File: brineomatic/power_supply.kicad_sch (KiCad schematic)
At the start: 26 parts, among them J8 5.08MM, J9 5.08MM, Q3 20N06, U2 LM74700, U3 XL1509-5.0

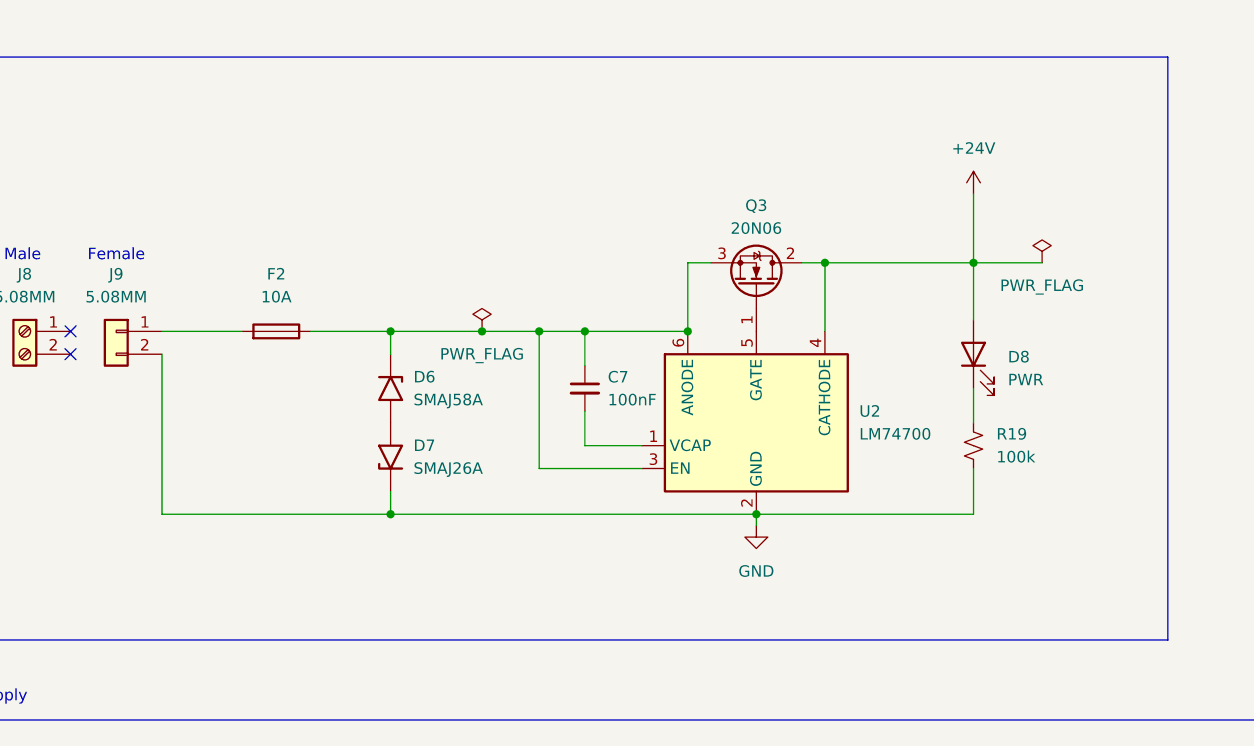
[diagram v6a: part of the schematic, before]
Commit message: removed the onboard fuse.
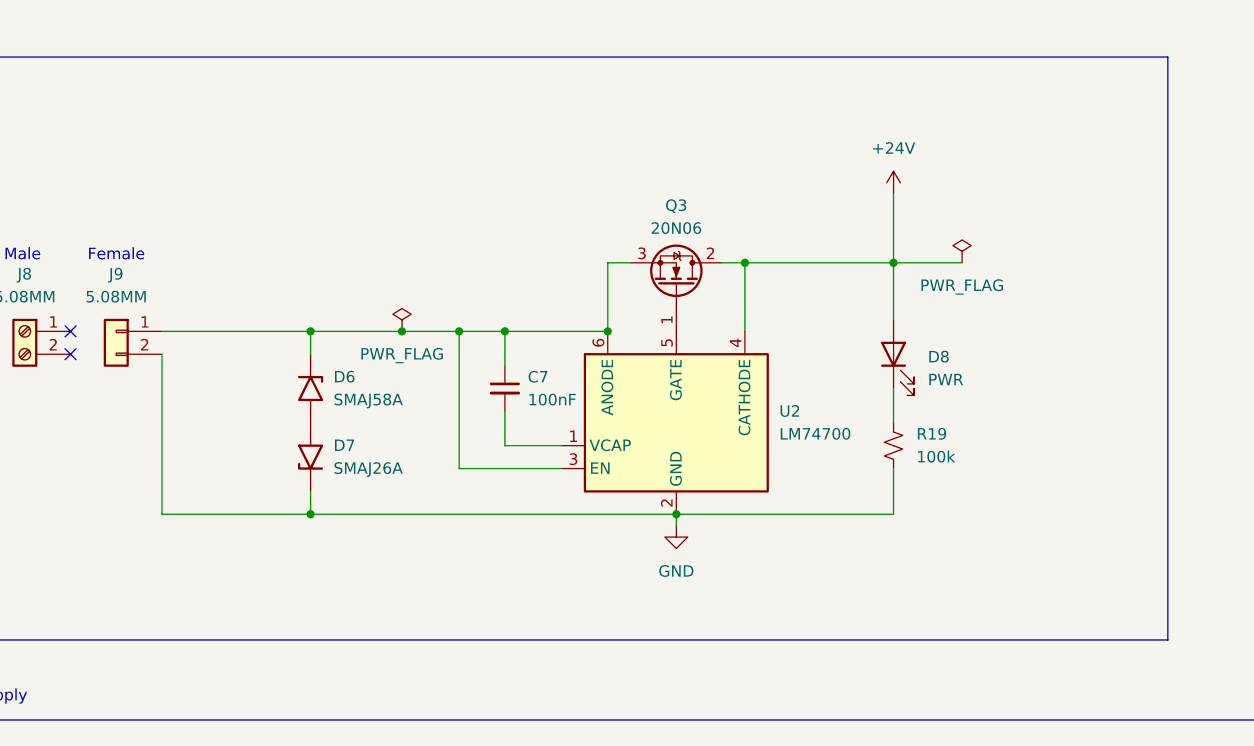
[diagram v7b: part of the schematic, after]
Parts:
- removed F2: 10A, yarrboard:FUSE-TH_XF-508P-A-B, symbol Device:Fuse
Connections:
- net at C7.1, D6.1 (A1), Q3.3 (S)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: now also J9.1 (Pin_1)
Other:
- moved on the sheet: C7, D6, D7, D8, Q3, R19, U2

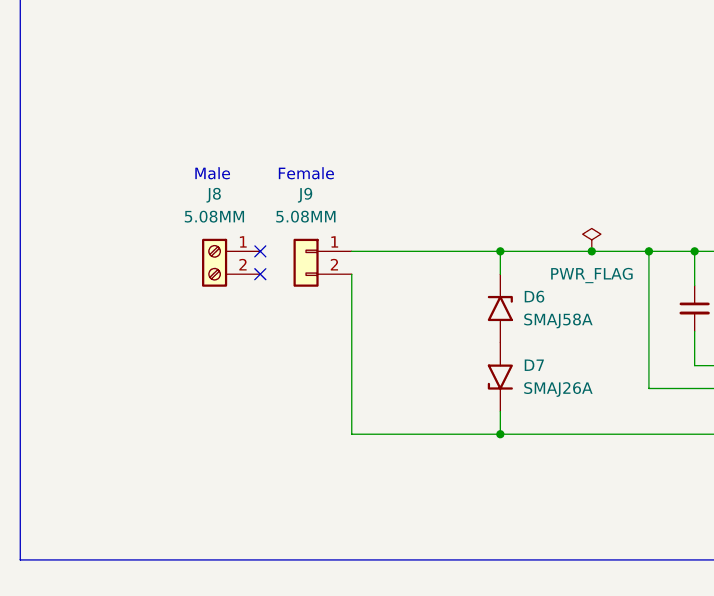
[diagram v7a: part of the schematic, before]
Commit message: re-added fuse, switched to 5x20mm
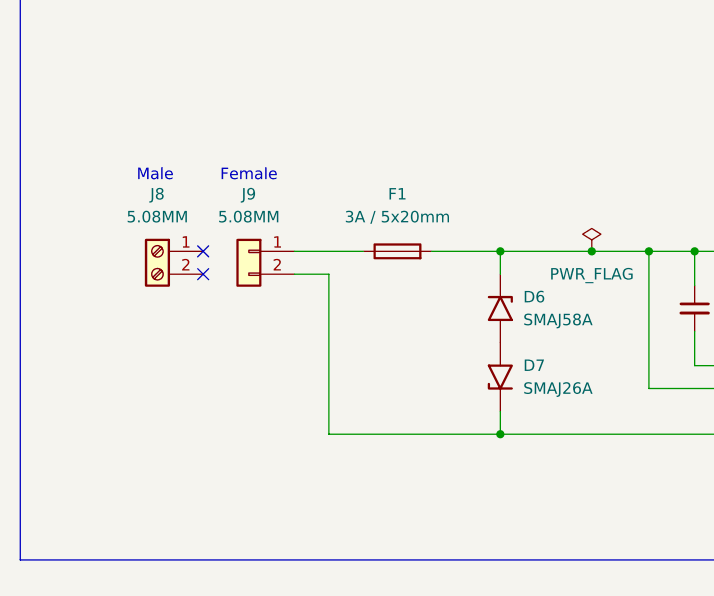
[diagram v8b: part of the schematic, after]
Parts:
- added F1: 3A / 5x20mm, yarrboard:Fuseholder_Cylinder-5x20mm_LittelFuse_646, symbol Device:Fuse
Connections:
- net at C7.1, D6.1 (A1), Q3.3 (S)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: now also F1.2; no longer J9.1 (Pin_1)
- new net: F1.1, J9.1 (Pin_1)
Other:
- moved on the sheet: J8, J9
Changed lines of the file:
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@@
 	(text "Male"
 		(exclude_from_sim no)
-		(at 42.926 44.45 0)
+		(at 36.576 44.45 0)
 		(effects
 			(font
@@
 	(text "Female"
 		(exclude_from_sim no)
-		(at 53.34 44.45 0)
+		(at 46.99 44.45 0)
 		(effects
 			(font
@@
 	)
 	(no_connect
-		(at 48.26 52.07)
+		(at 41.91 52.07)
 	)
 	(no_connect
-		(at 48.26 54.61)
+		(at 41.91 54.61)
 	)
 	(wire
@@
 	(wire
 		(pts
+			(xy 55.88 54.61) (xy 52.07 54.61)
+		)
+		(stroke
+			(width 0)
+			(type default)
+		)
+	)
+	(wire
+		(pts
 			(xy 118.11 134.62) (xy 118.11 137.16)
 		)
@@
 	(wire
 		(pts
-			(xy 58.42 72.39) (xy 58.42 54.61)
+			(xy 55.88 72.39) (xy 55.88 54.61)
 		)
 		(stroke
@@
 	(wire
 		(pts
-			(xy 58.42 52.07) (xy 74.93 52.07)
+			(xy 52.07 52.07) (xy 59.69 52.07)
 		)
 		(stroke
@@
 	(wire
 		(pts
+			(xy 67.31 52.07) (xy 74.93 52.07)
+		)
+		(stroke
+			(width 0)
+			(type default)
+		)
+	)
+	(wire
+		(pts
 			(xy 158.75 125.73) (xy 158.75 137.16)
 		)
@@
 	(wire
 		(pts
-			(xy 58.42 72.39) (xy 74.93 72.39)
+			(xy 55.88 72.39) (xy 74.93 72.39)
 		)
 		(stroke
@@
 	)
 	(symbol
+		(lib_id "Device:Fuse")
+		(at 63.5 52.07 90)
+		(unit 1)
+		(exclude_from_sim no)
+		(in_bom yes)
+		(on_board yes)
+		(dnp no)
+		(fields_autoplaced yes)
+		(property "Reference" "F1"
+			(at 63.5 45.72 90)
+			(effects
+				(font
+					(size 1.27 1.27)
+				)
+			)
+		)
+		(property "Value" "3A / 5x20mm"
+			(at 63.5 48.26 90)
+			(effects
+				(font
+					(size 1.27 1.27)
+				)
+			)
+		)
+		(property "Footprint" "yarrboard:Fuseholder_Cylinder-5x20mm_LittelFuse_646"
+			(at 63.5 53.848 90)
+			(effects
+				(font
+					(size 1.27 1.27)
+				)
+				(hide yes)
+			)
+		)
+		(property "Datasheet" "~"
+			(at 63.5 52.07 0)
+			(effects
+				(font
+					(size 1.27 1.27)
+				)
+				(hide yes)
+			)
+		)
+		(property "Description" "Fuse"
+			(at 63.5 52.07 0)
+			(effects
+				(font
+					(size 1.27 1.27)
+				)
+				(hide yes)
+			)
+		)
+		(property "LCSC" "C206887"
+			(at 63.5 52.07 90)
+			(effects
+				(font
+					(size 1.27 1.27)
+				)
+				(hide yes)
+			)
+		)
+		(property "Field6" ""
+			(at 63.5 52.07 90)
+			(effects
+				(font
+					(size 1.27 1.27)
+				)
+				(hide yes)
+			)
+		)
+		(pin "1"
+		)
+		(pin "2"
+		)
+		(instances
+			(project ""
+				(path "/96477ae2-ef08-48f3-8dd4-fe4478541f68/7cbb3b3c-cf93-4880-b816-c6df902b993c"
+					(reference "F1")
+					(unit 1)
+				)
+			)
+		)
+	)
+	(symbol
 		(lib_id "Device:C_Small")
 		(at 148.59 128.27 0)
@@
 	(symbol
 		(lib_id "Connector_Generic:Conn_01x02")
-		(at 53.34 52.07 0)
+		(at 46.99 52.07 0)
 		(mirror y)
 		(unit 1)
@@
 		(fields_autoplaced yes)
 		(property "Reference" "J9"
-			(at 53.34 45.72 0)
+			(at 46.99 45.72 0)
 			(effects
 				(font
@@
 		)
 		(property "Value" "5.08MM"
-			(at 53.34 48.26 0)
+			(at 46.99 48.26 0)
 			(effects
 				(font
@@
 		)
 		(property "Footprint" "Connector_Phoenix_MSTB:PhoenixContact_MSTBA_2,5_2-G-5,08_1x02_P5.08mm_Horizontal"
-			(at 53.34 52.07 0)
+			(at 46.99 52.07 0)
 			(effects
 				(font
@@
 		)
 		(property "Datasheet" "~"
-			(at 53.34 52.07 0)
+			(at 46.99 52.07 0)
 			(effects
 				(font
@@
 		)
 		(property "Description" "Generic connector, single row, 01x02, script generated (kicad-library-utils/schlib/autogen/connector/)"
-			(at 53.34 52.07 0)
+			(at 46.99 52.07 0)
 			(effects
 				(font
@@
 		)
 		(property "LCSC" "C3697"
-			(at 53.34 52.07 0)
+			(at 46.99 52.07 0)
 			(effects
 				(font
@@
 	(symbol
 		(lib_id "Connector:Screw_Terminal_01x02")
-		(at 43.18 52.07 0)
+		(at 36.83 52.07 0)
 		(mirror y)
 		(unit 1)
@@
 		(dnp no)
 		(property "Reference" "J8"
-			(at 43.18 45.72 0)
+			(at 36.83 45.72 0)
 			(effects
 				(font
@@
 		)
 		(property "Value" "5.08MM"
-			(at 43.18 48.26 0)
+			(at 36.83 48.26 0)
 			(effects
 				(font
@@
 		)
 		(property "Footprint" ""
-			(at 43.18 52.07 0)
+			(at 36.83 52.07 0)
 			(effects
 				(font
@@
 		)
 		(property "Datasheet" "~"
-			(at 43.18 52.07 0)
+			(at 36.83 52.07 0)
 			(effects
 				(font
@@
 		)
 		(property "Description" "Generic screw terminal, single row, 01x02, script generated (kicad-library-utils/schlib/autogen/connector/)"
-			(at 43.18 52.07 0)
+			(at 36.83 52.07 0)
 			(effects
 				(font
@@
 		)
 		(property "LCSC" "C71370"
-			(at 43.18 52.07 0)
+			(at 36.83 52.07 0)
 			(effects
 				(font
@@
 		)
 		(property "Field6" ""
-			(at 43.18 52.07 0)
+			(at 36.83 52.07 0)
 			(effects
 				(font
